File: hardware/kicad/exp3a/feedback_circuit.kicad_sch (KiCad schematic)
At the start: 8 parts, among them U1 IL300, U3 MCP601, U4 MCP601

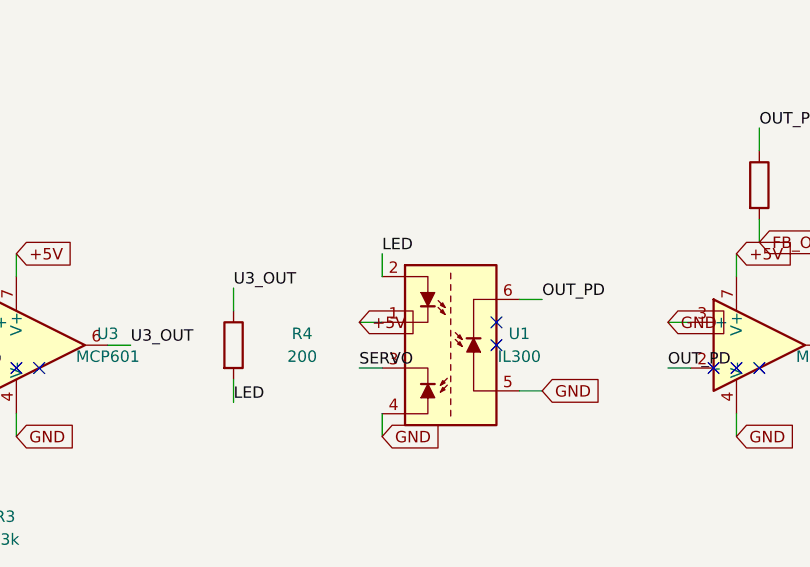
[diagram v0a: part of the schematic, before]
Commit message: Fix feedback servo polarity: drive IL300 LED anode-side from U3
Sim showed the as-drawn LED orientation (anode->+5V, cathode sunk by U3 with
+in=IN_P) is positive feedback and latches. Flip to anode<-R4<-U3, cathode->GND
so U3 sources the LED current -> negative feedback. Matches the validated
behavioral sim (FB_OUT = INPUT/6, linear).
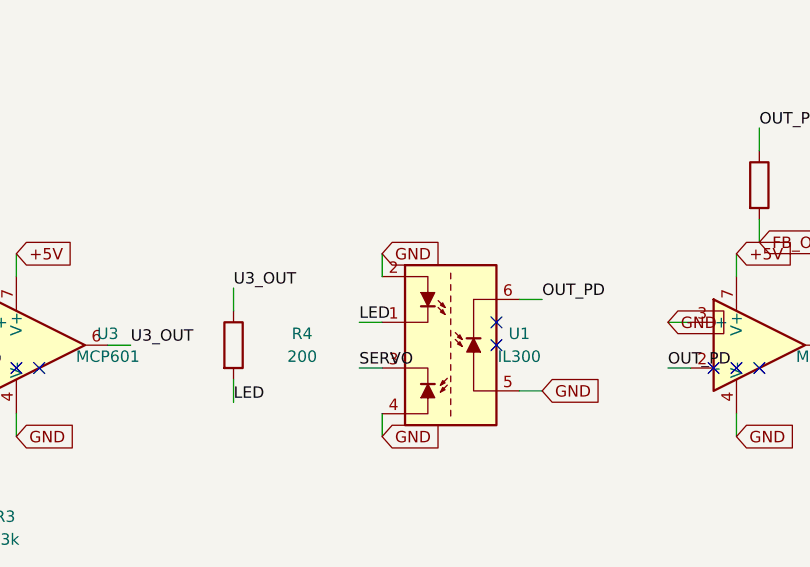
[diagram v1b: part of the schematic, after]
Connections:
- net +5V: no longer U1.1
- net GND: now also U1.2
- net LED: now also U1.1; no longer U1.2

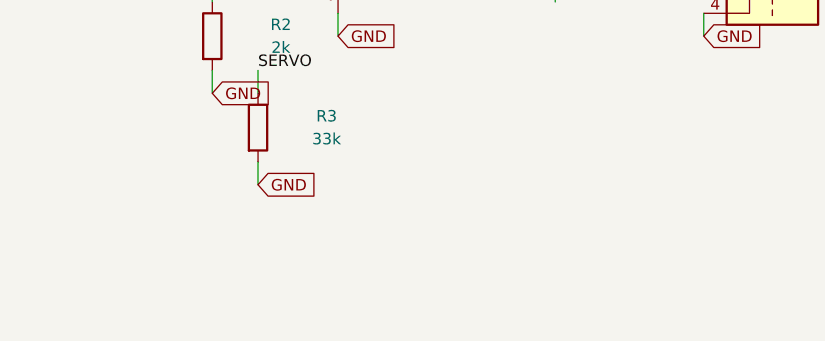
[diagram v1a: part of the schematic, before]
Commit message: Fix drive circuit wiring and make all four schematics PCB-ready
Two bugs from the GUI editing session fixed in drive_circuit:
- D1 (freewheel) had both pins on +20V (motor+ IS the +20V rail), so the
  motor had no flyback path at all. Anode moved to the switch node.
- The IR2110 HIN/SD/VSS/VS island was tied together but never reached
  GND - floating logic reference and undefined shutdown. Now grounded.

PCB-readiness for all four:
- buck/boost: removed the simulation-only V_in (SPICE VDC) and Rload,
  added screw terminals for power in/out plus headers for PWM (isolated
  GND_MCU) and the gate-drive rail. NOTE: buck's +12V_SW is referenced
  to the SW node (high-side switch -> floating supply needed).
- drive: PWM header + 3-pole supply terminal; motor lands on a 2-pole
  screw terminal.
- feedback: input/supply header + output header, PWR_FLAGs on +5V/GND.
- Every component now carries a verified footprint (see bom/).

retrofit_pcb.py documents/reproduces the whole edit. ERC after: 0 errors
on all four (feedback even 0 warnings).
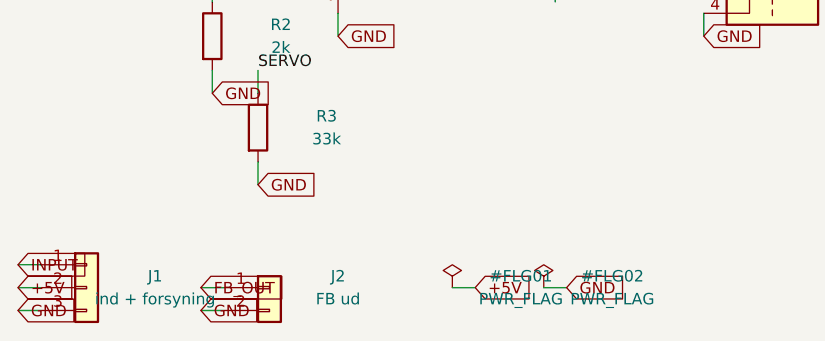
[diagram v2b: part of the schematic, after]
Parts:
- added J1: ind + forsyning, Connector_PinHeader_2.54mm:PinHeader_1x03_P2.54mm_Vertical, symbol Connector_Generic:Conn_01x03
- added J2: FB ud, Connector_PinHeader_2.54mm:PinHeader_1x02_P2.54mm_Vertical, symbol Connector_Generic:Conn_01x02
- R1, R2, R3, R4, R5: footprint (none) -> Resistor_THT:R_Axial_DIN0207_L6.3mm_D2.5mm_P7.62mm_Horizontal
- U1, U3, U4: footprint (none) -> Package_DIP:DIP-8_W7.62mm
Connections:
- net +5V: now also J1.2 (Pin_2)
- net FB_OUT: now also J2.1 (Pin_1)
- net GND: now also J1.3 (Pin_3), J2.2 (Pin_2)
- net INPUT: now also J1.1 (Pin_1)
